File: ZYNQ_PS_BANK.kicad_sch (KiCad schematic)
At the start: 4 parts, among them U1 XC7Z020-2CLG484I

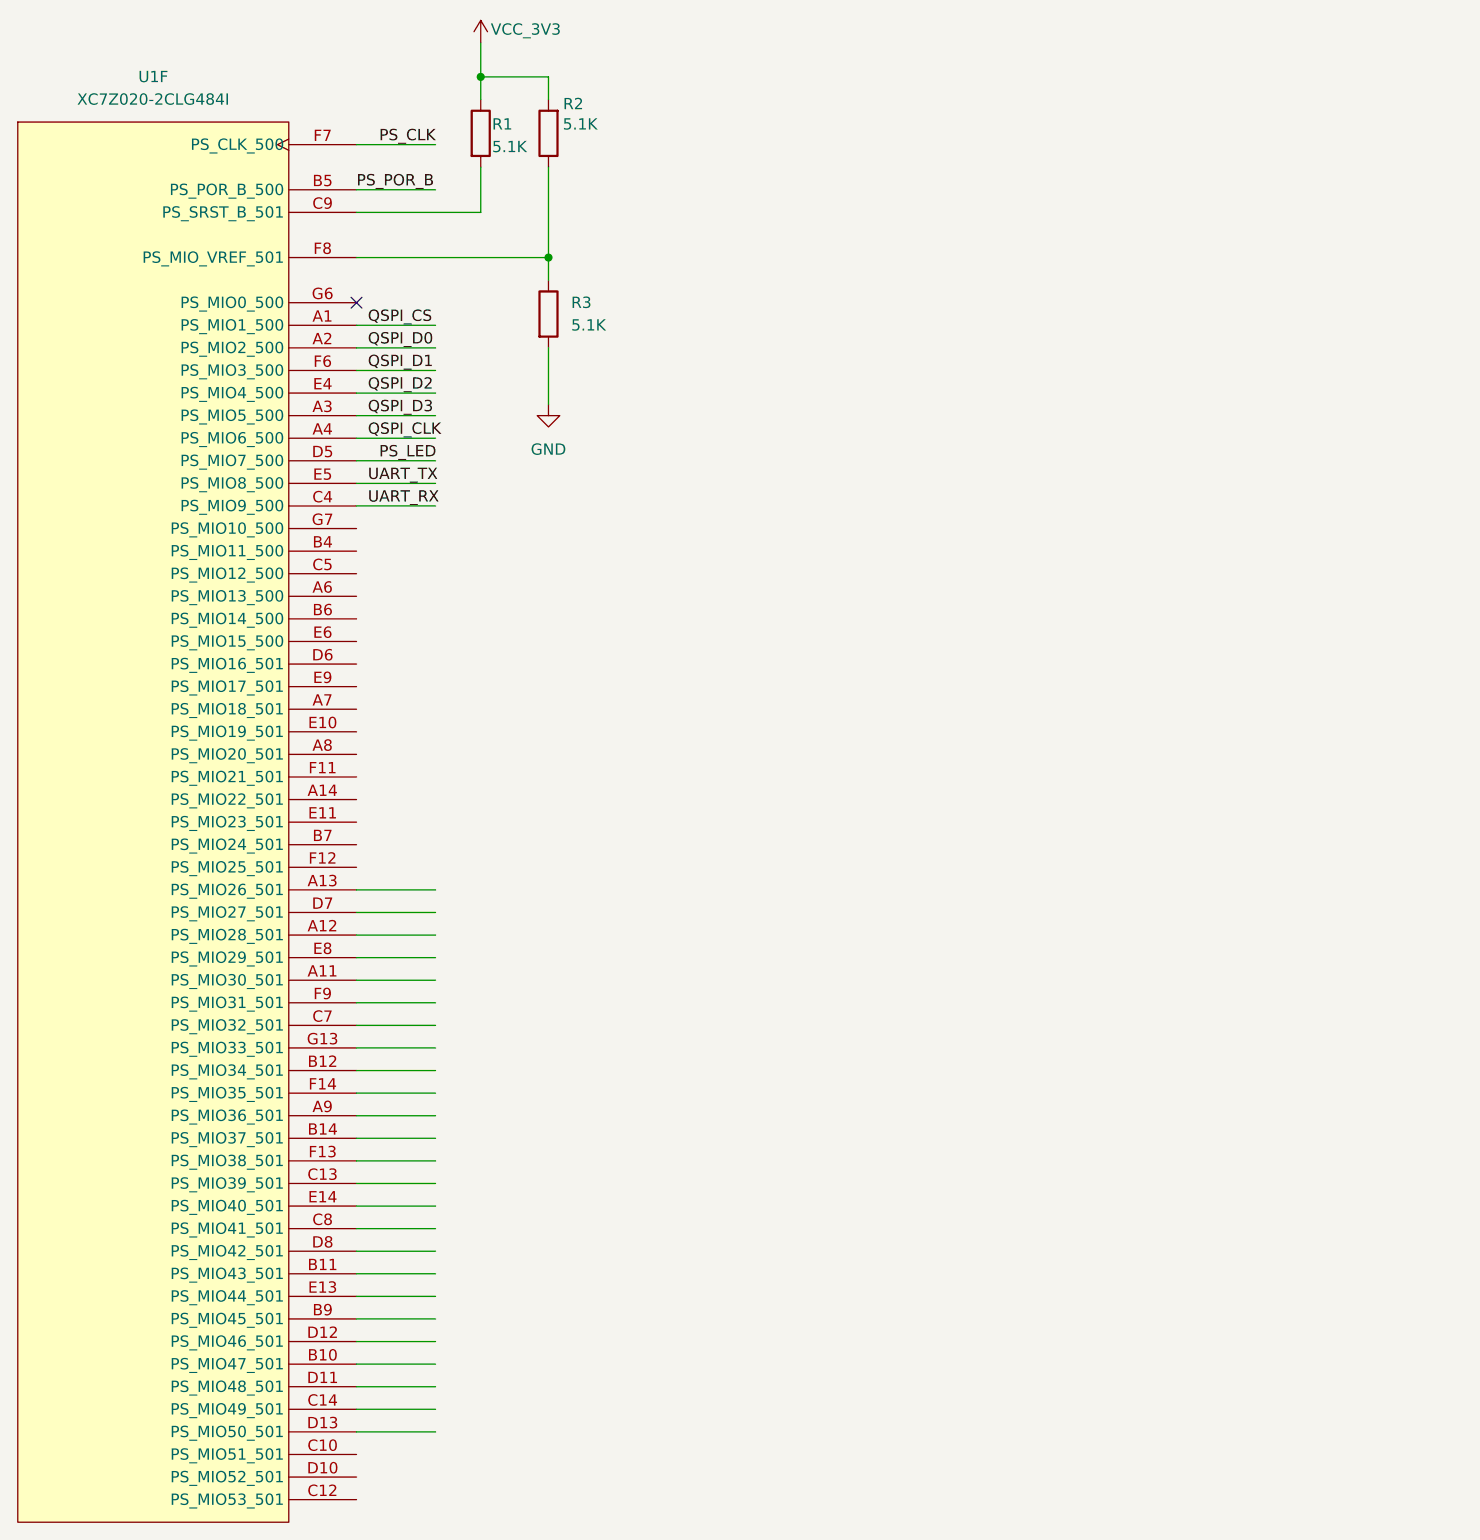
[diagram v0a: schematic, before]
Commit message: Update JTAG and SDR schematics and libraries
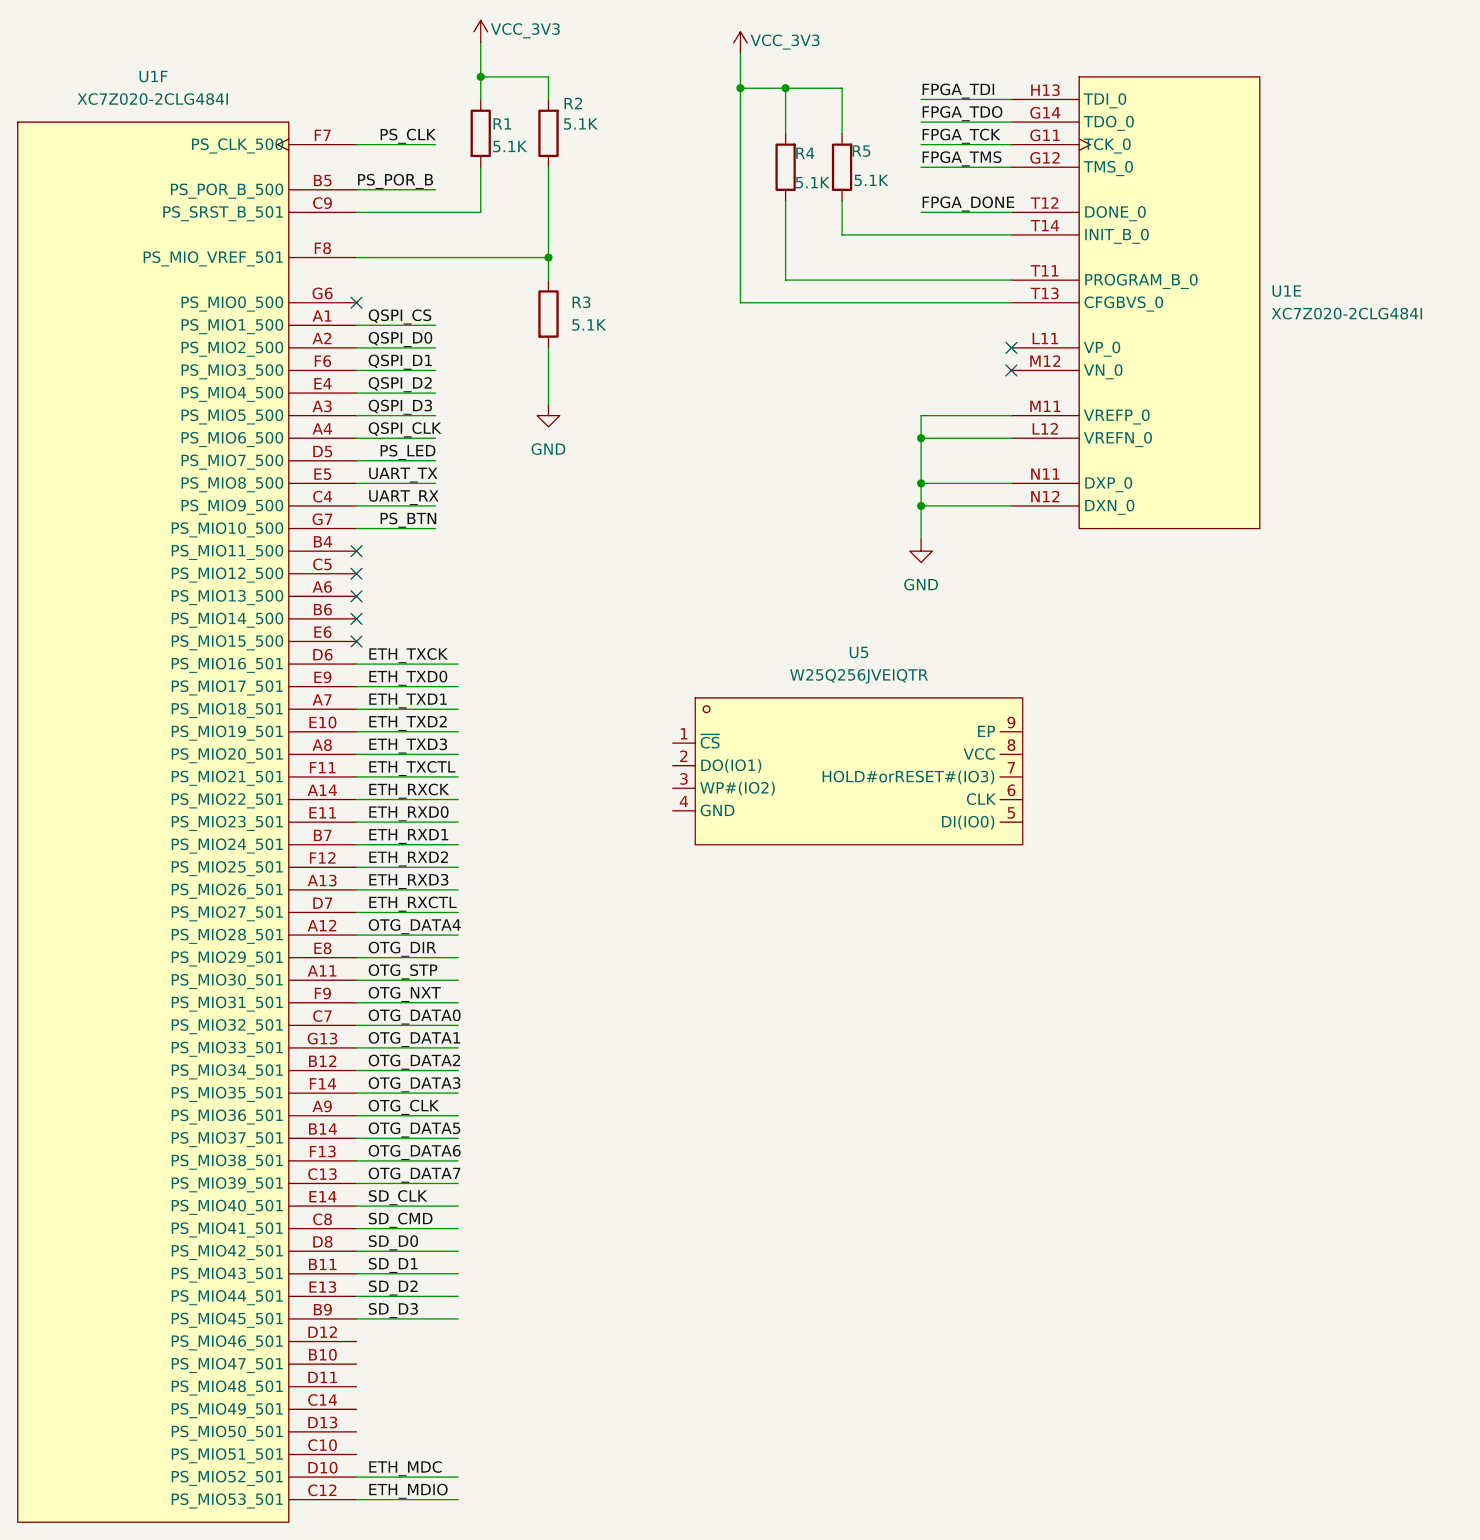
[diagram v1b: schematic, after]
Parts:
- added R4, R5: 5.1K, symbol Device:R
- added unit 5 of U1
- added U5: W25Q256JVEIQTR, easyeda2kicad:WSON-8_L8.0-W6.10-P1.27-BL-EP, symbol ZYNQ7020_SDR:W25Q256JVEIQTR
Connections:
- net GND: now also U1.L12 (VREFN_0), U1.M11 (VREFP_0), U1.N11 (DXP_0), U1.N12 (DXN_0)
- net VCC_3V3: now also R4.2, R5.2, U1.T13 (CFGBVS_0)
- net OTG_STP: now reaches U1.A11 (PS_MIO30_501)
- net OTG_DATA4: now reaches U1.A12 (PS_MIO28_501)
- net ETH_RXD3: now reaches U1.A13 (PS_MIO26_501)
- net ETH_RXCK: now reaches U1.A14 (PS_MIO22_501)
- net ETH_TXD1: now reaches U1.A7 (PS_MIO18_501)
- net ETH_TXD3: now reaches U1.A8 (PS_MIO20_501)
- net OTG_CLK: now reaches U1.A9 (PS_MIO36_501)
- net SD_D1: now reaches U1.B11 (PS_MIO43_501)
- net OTG_DATA2: now reaches U1.B12 (PS_MIO34_501)
- net OTG_DATA5: now reaches U1.B14 (PS_MIO37_501)
- net ETH_RXD1: now reaches U1.B7 (PS_MIO24_501)
- net SD_D3: now reaches U1.B9 (PS_MIO45_501)
- net ETH_MDIO: now reaches U1.C12 (PS_MIO53_501)
- net OTG_DATA7: now reaches U1.C13 (PS_MIO39_501)
- net OTG_DATA0: now reaches U1.C7 (PS_MIO32_501)
- net SD_CMD: now reaches U1.C8 (PS_MIO41_501)
- net ETH_MDC: now reaches U1.D10 (PS_MIO52_501)
- net ETH_TXCK: now reaches U1.D6 (PS_MIO16_501)
- net ETH_RXCTL: now reaches U1.D7 (PS_MIO27_501)
- net SD_D0: now reaches U1.D8 (PS_MIO42_501)
- net ETH_TXD2: now reaches U1.E10 (PS_MIO19_501)
- net ETH_RXD0: now reaches U1.E11 (PS_MIO23_501)
- net SD_D2: now reaches U1.E13 (PS_MIO44_501)
- net SD_CLK: now reaches U1.E14 (PS_MIO40_501)
- net OTG_DIR: now reaches U1.E8 (PS_MIO29_501)
- net ETH_TXD0: now reaches U1.E9 (PS_MIO17_501)
- net ETH_TXCTL: now reaches U1.F11 (PS_MIO21_501)
- net ETH_RXD2: now reaches U1.F12 (PS_MIO25_501)
- net OTG_DATA6: now reaches U1.F13 (PS_MIO38_501)
- net OTG_DATA3: now reaches U1.F14 (PS_MIO35_501)
- net OTG_NXT: now reaches U1.F9 (PS_MIO31_501)
- net OTG_DATA1: now reaches U1.G13 (PS_MIO33_501)
- net PS_BTN: now reaches U1.G7 (PS_MIO10_500)
- new net: R4.1, U1.T11 (PROGRAM_B_0)
- new net: R5.1, U1.T14 (INIT_B_0)
- new net FPGA_DONE: U1.T12 (DONE_0)
- new net FPGA_TCK: U1.G11 (TCK_0)
- new net FPGA_TDI: U1.H13 (TDI_0)
- new net FPGA_TDO: U1.G14 (TDO_0)
- new net FPGA_TMS: U1.G12 (TMS_0)
- no-connect marks 1 -> 8
